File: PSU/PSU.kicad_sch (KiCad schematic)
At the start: 26 parts, among them J1 12v_DC_OUT, J2 5v_DC_OUT, J3 9V_AC_OUT, J4 HDR1, Q1 VN4206A, T1 Transformer_Split_2x_9v, U1 LM7805_TO220, U2 MOC3041M

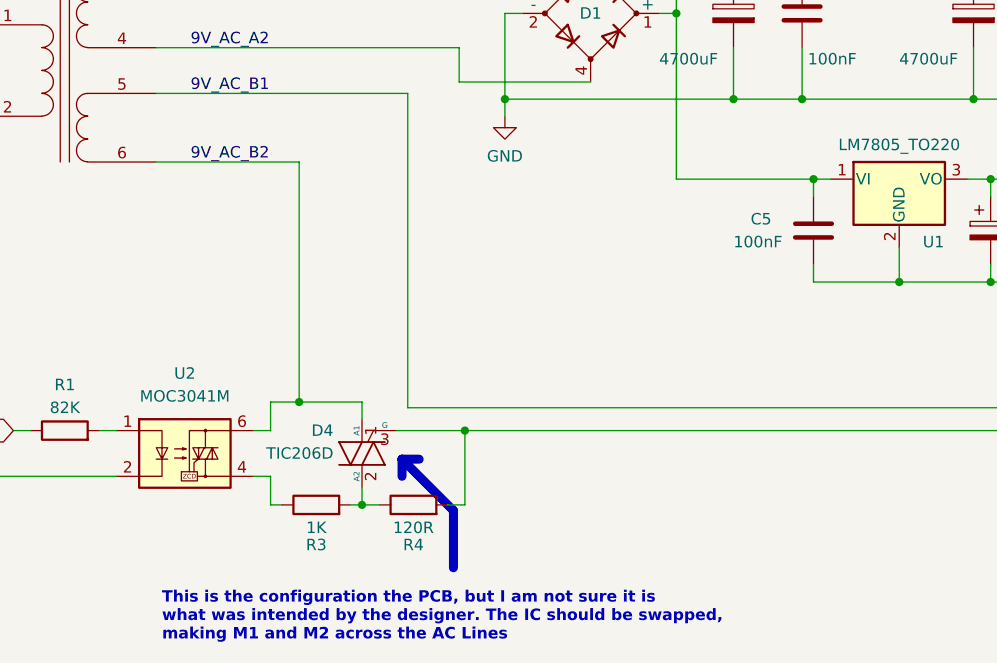
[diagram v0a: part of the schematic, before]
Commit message: Started EPROM Reader
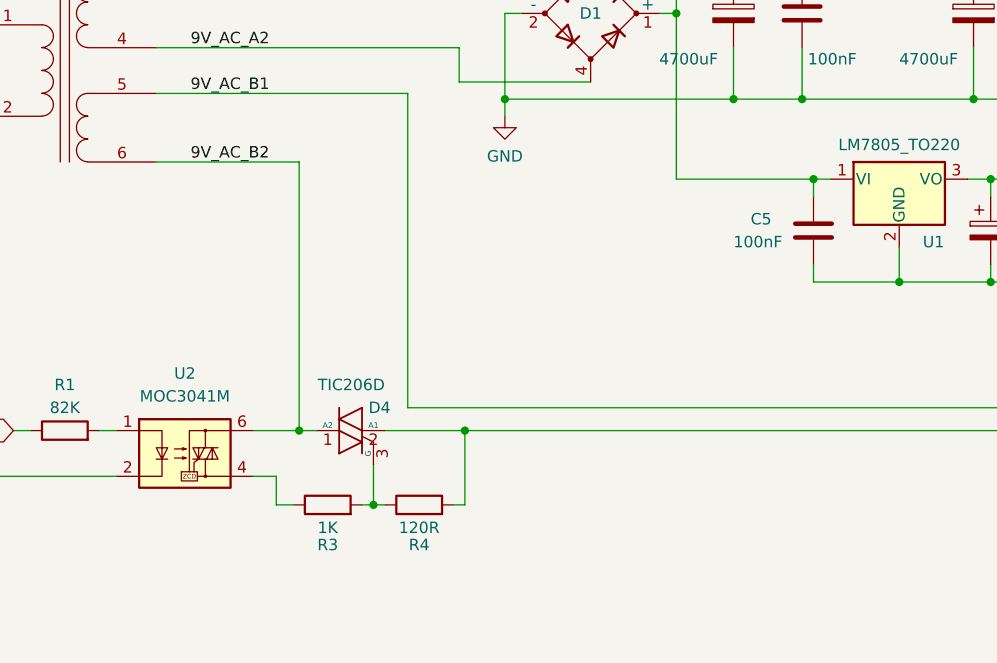
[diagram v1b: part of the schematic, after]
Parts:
- D4: symbol Device:Q_TRIAC_A1A2G -> Device:Q_TRIAC_A2A1G
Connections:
- net at R3.2, R4.1: now also D4.3 (G); no longer D4.2 (A2)
- net at J3.1 (Pin_1), R4.2: now also D4.2 (A1); no longer D4.3 (G)
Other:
- note removed: "This is the configuration the PCB, but I am not sure it is what was intended by the designer. The IC should be swapped, making M1 and M2 across the AC Lines"
- moved on the sheet: D4, R3, R4
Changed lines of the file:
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@@
   (junction (at 83.82 30.48) (diameter 0) (color 0 0 0 0)
   )
-  (junction (at 129.54 83.82) (diameter 0) (color 0 0 0 0)
+  (junction (at 122.555 75.565) (diameter 0) (color 0 0 0 0)
   )
   (junction (at 232.41 30.48) (diameter 0) (color 0 0 0 0)
@@
   (junction (at 75.565 40.64) (diameter 0) (color 0 0 0 0)
   )
-  (junction (at 122.555 72.39) (diameter 0) (color 0 0 0 0)
+  (junction (at 130.81 83.82) (diameter 0) (color 0 0 0 0)
   )
   (junction (at 140.97 75.565) (diameter 0) (color 0 0 0 0)
@@
     (stroke (width 0) (type default))
   )
-  (wire (pts (xy 122.555 72.39) (xy 129.54 72.39))
-    (stroke (width 0) (type default))
-  )
   (wire (pts (xy 199.39 59.055) (xy 189.23 59.055))
     (stroke (width 0) (type default))
@@
     (stroke (width 0) (type default))
   )
-  (wire (pts (xy 119.38 72.39) (xy 119.38 75.565))
+  (wire (pts (xy 122.555 45.72) (xy 122.555 75.565))
     (stroke (width 0) (type default))
   )
@@
     (stroke (width 0) (type default))
   )
-  (wire (pts (xy 117.475 80.645) (xy 119.38 80.645))
+  (wire (pts (xy 117.475 80.645) (xy 120.015 80.645))
     (stroke (width 0) (type default))
   )
@@
     (stroke (width 0) (type default))
   )
+  (wire (pts (xy 130.81 79.375) (xy 130.81 83.82))
+    (stroke (width 0) (type default))
+  )
   (wire (pts (xy 232.41 50.165) (xy 232.41 59.055))
     (stroke (width 0) (type default))
@@
     (stroke (width 0) (type default))
   )
-  (wire (pts (xy 129.54 72.39) (xy 129.54 74.295))
-    (stroke (width 0) (type default))
-  )
   (wire (pts (xy 213.36 30.48) (xy 232.41 30.48))
     (stroke (width 0) (type default))
@@
     (stroke (width 0) (type default))
   )
-  (wire (pts (xy 139.065 83.82) (xy 140.97 83.82))
-    (stroke (width 0) (type default))
-  )
-  (wire (pts (xy 122.555 45.72) (xy 122.555 72.39))
-    (stroke (width 0) (type default))
-  )
-  (wire (pts (xy 117.475 75.565) (xy 119.38 75.565))
+  (wire (pts (xy 139.7 83.82) (xy 140.97 83.82))
+    (stroke (width 0) (type default))
+  )
+  (wire (pts (xy 117.475 75.565) (xy 122.555 75.565))
     (stroke (width 0) (type default))
   )
@@
     (stroke (width 0) (type default))
   )
-  (wire (pts (xy 119.38 83.82) (xy 120.65 83.82))
+  (wire (pts (xy 120.015 83.82) (xy 121.92 83.82))
     (stroke (width 0) (type default))
   )
@@
     (stroke (width 0) (type default))
   )
-  (wire (pts (xy 129.54 83.82) (xy 131.445 83.82))
-    (stroke (width 0) (type default))
-  )
   (wire (pts (xy 52.07 54.61) (xy 83.82 54.61))
     (stroke (width 0) (type default))
@@
     (stroke (width 0) (type default))
   )
+  (wire (pts (xy 122.555 75.565) (xy 124.46 75.565))
+    (stroke (width 0) (type default))
+  )
   (wire (pts (xy 164.465 29.21) (xy 164.465 47.625))
     (stroke (width 0) (type default))
@@
     (stroke (width 0) (type default))
   )
-  (polyline (pts (xy 139.7 90.805) (xy 139.7 84.455))
-    (stroke (width 1) (type default))
-  )
   (wire (pts (xy 100.33 75.565) (xy 102.235 75.565))
     (stroke (width 0) (type default))
@@
     (stroke (width 0) (type default))
   )
-  (wire (pts (xy 129.54 83.82) (xy 129.54 81.915))
-    (stroke (width 0) (type default))
-  )
-  (polyline (pts (xy 133.985 78.74) (xy 133.985 80.645))
-    (stroke (width 1) (type default))
-  )
-  (polyline (pts (xy 133.985 78.74) (xy 135.89 78.74))
-    (stroke (width 1) (type default))
-  )
   (wire (pts (xy 199.39 47.625) (xy 199.39 49.53))
     (stroke (width 0) (type default))
@@
     (stroke (width 0) (type default))
   )
+  (wire (pts (xy 130.81 83.82) (xy 132.08 83.82))
+    (stroke (width 0) (type default))
+  )
   (wire (pts (xy 199.39 57.15) (xy 199.39 59.055))
     (stroke (width 0) (type default))
   )
-  (wire (pts (xy 133.35 75.565) (xy 140.97 75.565))
+  (wire (pts (xy 132.08 75.565) (xy 140.97 75.565))
     (stroke (width 0) (type default))
   )
@@
     (stroke (width 0) (type default))
   )
-  (wire (pts (xy 119.38 72.39) (xy 122.555 72.39))
-    (stroke (width 0) (type default))
-  )
   (wire (pts (xy 67.945 69.215) (xy 69.215 69.215))
     (stroke (width 0) (type default))
@@
     (stroke (width 0) (type default))
   )
-  (wire (pts (xy 119.38 80.645) (xy 119.38 83.82))
+  (wire (pts (xy 120.015 80.645) (xy 120.015 83.82))
     (stroke (width 0) (type default))
   )
@@
     (stroke (width 0) (type default))
   )
-  (polyline (pts (xy 139.7 84.455) (xy 133.985 78.74))
-    (stroke (width 1) (type default))
-  )
   (wire (pts (xy 170.815 33.02) (xy 170.815 38.735))
     (stroke (width 0) (type default))
@@
     (stroke (width 0) (type default))
   )
-  (wire (pts (xy 128.27 83.82) (xy 129.54 83.82))
+  (wire (pts (xy 129.54 83.82) (xy 130.81 83.82))
     (stroke (width 0) (type default))
   )
@@
   (wire (pts (xy 134.62 38.1) (xy 134.62 73.025))
     (stroke (width 0) (type default))
-  )
-  (text "This is the configuration the PCB, but I am not sure it is\nwhat was intended by the designer. The IC should be swapped,\nmaking M1 and M2 across the AC Lines"
-    (at 107.315 99.06 0)
-    (effects (font (size 1.27 1.27) (thickness 0.254) bold) (justify left bottom))
   )
   (label "9V_DC" (at 171.45 19.685 0) (fields_autoplaced)
@@
     )
   )
-  (symbol (lib_id "Device:R") (at 135.255 83.82 90) (unit 1)
-    (in_bom yes) (on_board yes) (dnp no)
-    (property "Reference" "R4" (at 135.255 88.265 90)
-      (effects (font (size 1.27 1.27)))
-    )
-    (property "Value" "120R" (at 135.255 86.36 90)
-      (effects (font (size 1.27 1.27)))
-    )
-    (property "Footprint" "" (at 135.255 85.598 90)
-      (effects (font (size 1.27 1.27)) hide)
-    )
-    (property "Datasheet" "~" (at 135.255 83.82 0)
+  (symbol (lib_id "Device:R") (at 135.89 83.82 90) (unit 1)
+    (in_bom yes) (on_board yes) (dnp no)
+    (property "Reference" "R4" (at 135.89 88.265 90)
+      (effects (font (size 1.27 1.27)))
+    )
+    (property "Value" "120R" (at 135.89 86.36 90)
+      (effects (font (size 1.27 1.27)))
+    )
+    (property "Footprint" "" (at 135.89 85.598 90)
+      (effects (font (size 1.27 1.27)) hide)
+    )
+    (property "Datasheet" "~" (at 135.89 83.82 0)
       (effects (font (size 1.27 1.27)) hide)
     )
@@
     )
   )
-  (symbol (lib_id "Device:R") (at 124.46 83.82 90) (unit 1)
-    (in_bom yes) (on_board yes) (dnp no)
-    (property "Reference" "R3" (at 124.46 88.265 90)
-      (effects (font (size 1.27 1.27)))
-    )
-    (property "Value" "1K" (at 124.46 86.36 90)
-      (effects (font (size 1.27 1.27)))
-    )
-    (property "Footprint" "" (at 124.46 85.598 90)
-      (effects (font (size 1.27 1.27)) hide)
-    )
-    (property "Datasheet" "~" (at 124.46 83.82 0)
+  (symbol (lib_id "Device:R") (at 125.73 83.82 90) (unit 1)
+    (in_bom yes) (on_board yes) (dnp no)
+    (property "Reference" "R3" (at 125.73 88.265 90)
+      (effects (font (size 1.27 1.27)))
+    )
+    (property "Value" "1K" (at 125.73 86.36 90)
+      (effects (font (size 1.27 1.27)))
+    )
+    (property "Footprint" "" (at 125.73 85.598 90)
+      (effects (font (size 1.27 1.27)) hide)
+    )
+    (property "Datasheet" "~" (at 125.73 83.82 0)
       (effects (font (size 1.27 1.27)) hide)
     )
@@
     )
   )
-  (symbol (lib_id "Device:Q_TRIAC_A1A2G") (at 129.54 78.105 180) (unit 1)
-    (in_bom yes) (on_board yes) (dnp no)
-    (property "Reference" "D4" (at 126.365 75.565 0)
-      (effects (font (size 1.27 1.27)) (justify left))
-    )
-    (property "Value" "TIC206D" (at 126.365 78.105 0)
-      (effects (font (size 1.27 1.27)) (justify left))
-    )
-    (property "Footprint" "" (at 127.635 78.74 90)
-      (effects (font (size 1.27 1.27)) hide)
-    )
-    (property "Datasheet" "~" (at 129.54 78.105 90)
-      (effects (font (size 1.27 1.27)) hide)
-    )
+  (symbol (lib_id "Device:Q_TRIAC_A2A1G") (at 128.27 75.565 90) (unit 1)
+    (in_bom yes) (on_board yes) (dnp no)
+    (property "Reference" "D4" (at 132.715 73.025 90)
+      (effects (font (size 1.27 1.27)) (justify left))
+    )
+    (property "Value" "TIC206D" (at 132.08 70.485 90)
+      (effects (font (size 1.27 1.27)) (justify left))
+    )
+    (property "Footprint" "" (at 127.635 73.66 90)
+      (effects (font (size 1.27 1.27)) hide)
+    )
+    (property "Datasheet" "~" (at 128.27 75.565 90)
+      (effects (font (size 1.27 1.27)) hide)
+    )
